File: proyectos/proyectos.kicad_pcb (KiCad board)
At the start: 2 copper layers, 55.9 x 30.2 mm, 54 parts, among them P1 CONN_01X02, P2 CONN_01X03, P3 CONN_01X05, P4 CONN_01X03, P5 CONN_01X03, P6 CONN_01X02, U1 AD8232_A, U2 ADP3303-3.3, U3 PIC16F688, Y1 Crystal_8MHz

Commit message: VERSION 1.7 ECG Y PIC
NUEVA VERSION
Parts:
- added P7: CONN_01X01, Huellas:MountingHole_1.8mm_Pad, F.Cu at (119.9, 86.6)
- added P8: CONN_01X01, Huellas:MountingHole_1.8mm_Pad, F.Cu at (171.2, 86.6)
- moved P4 3.02 mm to (166.7, 86.1), turned to 0 degrees
- moved D2 2.09 mm to (123.9, 90.0), turned to 270 degrees
- moved R18 1.56 mm to (126.4, 90.0), turned to 270 degrees
- moved D3 0.69 mm to (163.1, 88.4)
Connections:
- P4 pad 1: /O_DIG1 -> /GND
- P4 pad 2: /O_DIG2 -> /O_DIG1
- P4 pad 3: /GND -> /O_DIG2
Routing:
- net /GND: track 150.3 -> 175.9 mm, vias 46 -> 53
- net /O_DIG2: track 11.8 -> 7.50 mm
- net +vs: track 92.2 -> 93.1 mm
- net Net-(D2-Pad2): track 3.47 -> 2.61 mm
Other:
- board size 55.9 x 30.2 mm -> 55.9 x 31 mm

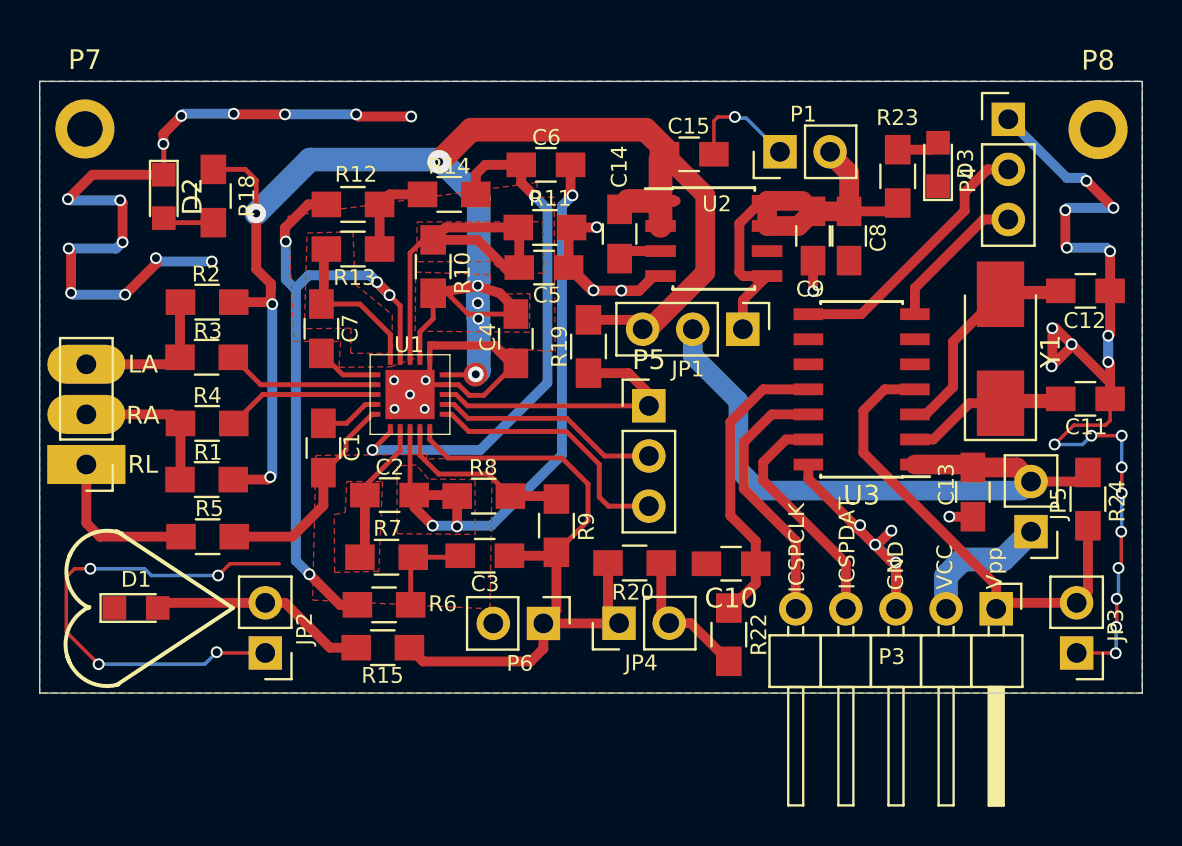
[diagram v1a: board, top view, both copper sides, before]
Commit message: VERSION 1.8 ECG Y PIC
CAMBIO DE REGULADOR POR ADP3334
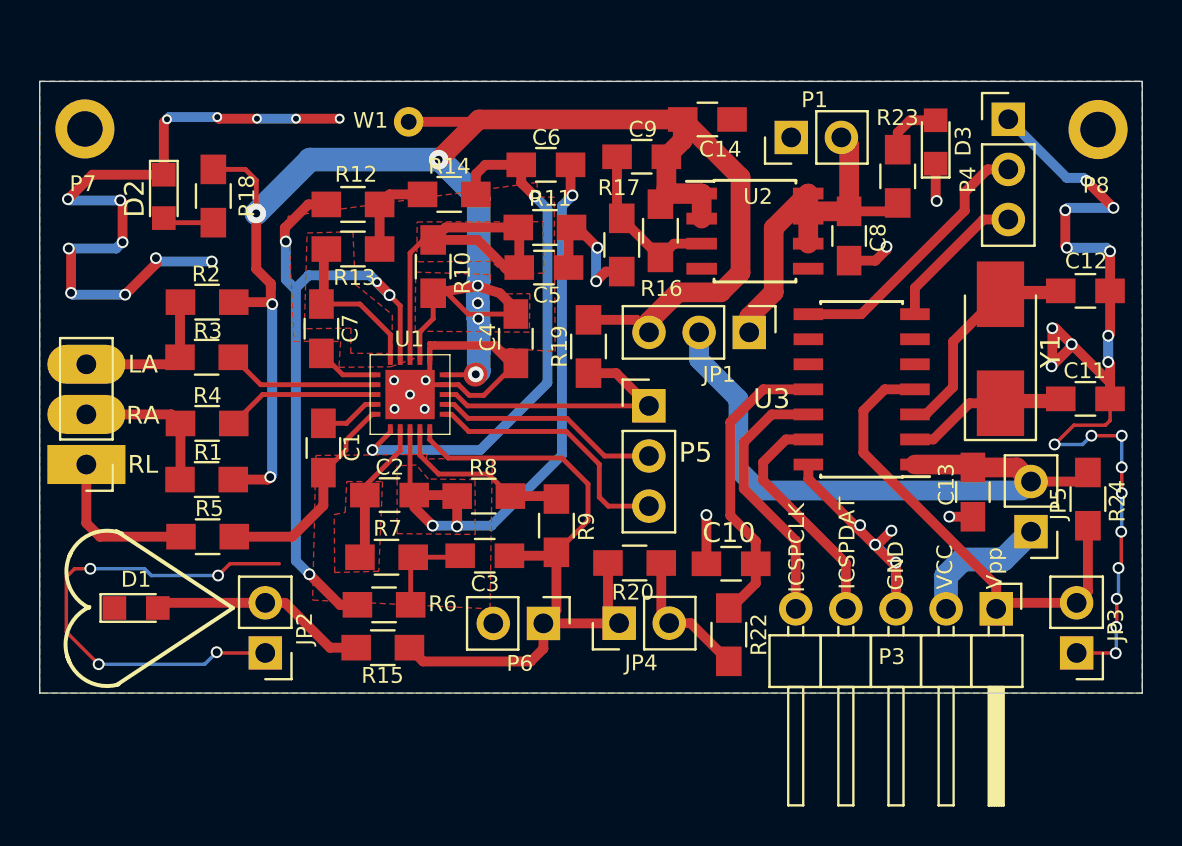
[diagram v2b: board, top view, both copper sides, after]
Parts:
- removed C15: 4.7uF, Capacitors_SMD:C_0805_HandSoldering
- added R16: 140K, Resistors_SMD:R_0805_HandSoldering, F.Cu at (149.1, 91.8)
- added R17: 78.7K, Resistors_SMD:R_0805_HandSoldering, F.Cu at (147.1, 92.5)
- added W1: TEST_1P, Measurement_Points:Measurement_Point_Round-TH_Small, F.Cu at (136.3, 86.2)
- C14: value 0.1uF -> 1uF
- C8: value 10uF -> 1uF
- U2: value ADP3303-3.3 -> ADP3334
- moved C9 9.57 mm to (148.1, 88.0), turned to 180 degrees
- moved C14 7.31 mm to (151.4, 86.1), turned to 0 degrees
- moved U2 2.12 mm to (153.9, 91.8)
- moved D3 1.15 mm to (163.0, 87.3)
- moved P1 0.93 mm to (155.7, 87.0)
- moved JP1 0.36 mm to (153.6, 96.9)
- turned C11 to 0 degrees
- turned C12 to 0 degrees
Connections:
- C11 pad 1: /GND -> Net-(C11-Pad1)
- C11 pad 2: Net-(C11-Pad2) -> /GND
- C12 pad 1: /GND -> Net-(C12-Pad1)
- C12 pad 2: Net-(C12-Pad2) -> /GND
- C14 pad 1: Net-(C14-Pad1) -> +vs
- C14 pad 2: +vs -> /GND
- C9 pad 1: /+5V -> +vs
- C9 pad 2: /GND -> Net-(C9-Pad2)
- U2 pad 3: Net-(C14-Pad1) -> Net-(C9-Pad2)
- U2 pad 4: /GND -> (no net)
- U2 pad 5: /+5V -> /GND
- U2 pad 6: (no net) -> /+5V
- U3 pad 2: Net-(C11-Pad2) -> Net-(C11-Pad1)
- U3 pad 3: Net-(C12-Pad2) -> Net-(C12-Pad1)
- Y1 pad 1: Net-(C11-Pad2) -> Net-(C11-Pad1)
- Y1 pad 2: Net-(C12-Pad2) -> Net-(C12-Pad1)
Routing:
- net Net-(C12-Pad2): track 14.5 -> 0.00 mm
- net Net-(C12-Pad1): track 0.00 -> 14.5 mm
- net +vs: track 93.1 -> 104.9 mm
- net Net-(C11-Pad2): track 11.4 -> 0.00 mm
- net Net-(C11-Pad1): track 0.00 -> 11.4 mm
- net /GND: track 175.9 -> 166.4 mm, vias 53 -> 52
- net Net-(C9-Pad2): track 0.00 -> 8.39 mm
- net /+5V: track 23.6 -> 19.6 mm
- net Net-(C14-Pad1): track 2.24 -> 0.00 mm
- net Net-(D3-Pad2): track 2.19 -> 3.05 mm

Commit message: version 1.9 ECG Y PIC
nuevo cambio de regulador  y logo
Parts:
- C14: moved to B.Cu
- C9: value 0.1uF -> 1nF_1208; footprint Capacitors_SMD:C_0805_HandSoldering -> Capacitors_SMD:C_1206_HandSoldering
- moved C14 2.44 mm to (149.8, 87.9), turned to 180 degrees
- moved W1 1.48 mm to (137.8, 85.9)
- moved C9 0.80 mm to (148.9, 87.9)
- moved C8 0.51 mm to (158.9, 91.6)
- turned U2 to 180 degrees
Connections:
- U2 pad 1: +vs -> /GND
- U2 pad 2: +vs -> /GND
- U2 pad 3: Net-(C9-Pad2) -> /+5V
- U2 pad 4: (no net) -> /+5V
- U2 pad 5: /GND -> +vs
- U2 pad 6: /+5V -> +vs
- U2 pad 7: /+5V -> Net-(C9-Pad2)
- U2 pad 8: /+5V -> (no net)
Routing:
- net /GND: track 166.4 -> 184.6 mm, vias 52 -> 59
- net +vs: track 104.9 -> 103.1 mm, vias 8 -> 9
- net /+5V: track 19.6 -> 21.2 mm
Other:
- board text added: "ONE"
- board text added: "SBS"
- board text added: "SBS Module : 002"

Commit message: version 2.0 ecg y pic
archivo para panelizar
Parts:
- removed P7, P8: CONN_01X01, Huellas:MountingHole_1.8mm_Pad
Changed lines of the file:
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@@
     (area 117.587599 84.175899 173.493001 115.201301)
     (thickness 1.6)
-    (drawings 33)
+    (drawings 31)
     (tracks 569)
     (zones 0)
-    (modules 58)
+    (modules 56)
     (nets 40)
   )
@@
   (layers
     (0 F.Cu signal)
-    (31 B.Cu signal hide)
+    (31 B.Cu signal)
     (32 B.Adhes user)
     (33 F.Adhes user)
@@
       (padsonsilk false)
       (subtractmaskfromsilk false)
-      (outputformat 1)
+      (outputformat 4)
       (mirror false)
       (drillshape 0)
       (scaleselection 1)
-      (outputdirectory "../../Desktop/PROYECTO GRADO/GALERIA_imagenes/gerber/"))
+      (outputdirectory "../../../../Desktop/PROYECTO GRADO/GALERIA_imagenes/gerber/"))
   )
   (net 0 "")
@@
     )
   )
-  (module Huellas:MountingHole_1.8mm_Pad (layer F.Cu)
-    (at 119.8903 86.5986)
-    (descr "Mounting Hole 2.5mm")
-    (tags "mounting hole 2.5mm")
-    (fp_text reference P7 (at -0.1 2.78) (layer F.SilkS)
-      (effects (font (size 0.8 0.8) (thickness 0.15)))
-    )
-    (fp_text value CONN_01X01 (at 0 3.5) (layer F.Fab) hide
-      (effects (font (size 1 1) (thickness 0.15)))
-    )
-    (pad 1 thru_hole circle (at 0 0) (size 3 3) (drill 1.8) (layers *.Cu *.Mask F.SilkS))
-  )
-  (module Huellas:MountingHole_1.8mm_Pad (layer F.Cu)
-    (at 171.2403 86.6286)
-    (descr "Mounting Hole 2.5mm")
-    (tags "mounting hole 2.5mm")
-    (fp_text reference P8 (at 0.58 2.28) (layer F.SilkS)
-      (effects (font (size 0.8 0.8) (thickness 0.15)))
-    )
-    (fp_text value CONN_01X01 (at 0 3.5) (layer F.Fab) hide
-      (effects (font (size 1 1) (thickness 0.15)))
-    )
-    (pad 1 thru_hole circle (at 0 0) (size 3 3) (drill 1.8) (layers *.Cu *.Mask F.SilkS))
-  )
   (module Resistors_SMD:R_0805_HandSoldering (layer F.Cu)
     (at 149.0603 91.7586 270)
@@
   (gr_line (start 117.6003 115.1886) (end 173.4803 115.1886) (angle 90) (layer Edge.Cuts) (width 0.0254))
   (gr_line (start 117.6003 84.1886) (end 117.6003 115.1886) (angle 90) (layer Edge.Cuts) (width 0.0254))
-  (dimension 31 (width 0.3) (layer F.SilkS)
-    (gr_text 31.000mm (at 110.160301 99.6886 270) (layer F.SilkS)
-      (effects (font (size 1.5 1.5) (thickness 0.3)))
-    )
-    (feature1 (pts (xy 117.6003 115.1886) (xy 108.810301 115.1886)))
-    (feature2 (pts (xy 117.6003 84.1886) (xy 108.810301 84.1886)))
-    (crossbar (pts (xy 111.510301 84.1886) (xy 111.510301 115.1886)))
-    (arrow1a (pts (xy 111.510301 115.1886) (xy 110.92388 114.062096)))
-    (arrow1b (pts (xy 111.510301 115.1886) (xy 112.096722 114.062096)))
-    (arrow2a (pts (xy 111.510301 84.1886) (xy 110.92388 85.315104)))
-    (arrow2b (pts (xy 111.510301 84.1886) (xy 112.096722 85.315104)))
-  )
   (gr_text Vpp (at 166.0003 108.4286 90) (layer F.SilkS)
     (effects (font (size 0.8 0.8) (thickness 0.125)))
@@
     (effects (font (size 1.5 1.5) (thickness 0.3)) (justify mirror))
   )
-  (dimension 55.88 (width 0.3) (layer F.SilkS)
-    (gr_text 55.880mm (at 145.542 126.2926) (layer F.SilkS)
-      (effects (font (size 1.5 1.5) (thickness 0.3)))
-    )
-    (feature1 (pts (xy 117.602 115.189) (xy 117.602 127.6426)))
-    (feature2 (pts (xy 173.482 115.189) (xy 173.482 127.6426)))
-    (crossbar (pts (xy 173.482 124.9426) (xy 117.602 124.9426)))
-    (arrow1a (pts (xy 117.602 124.9426) (xy 118.728504 124.356179)))
-    (arrow1b (pts (xy 117.602 124.9426) (xy 118.728504 125.529021)))
-    (arrow2a (pts (xy 173.482 124.9426) (xy 172.355496 124.356179)))
-    (arrow2b (pts (xy 173.482 124.9426) (xy 172.355496 125.529021)))
-  )
   (gr_text RA (at 122.8344 101.1174) (layer F.SilkS)
